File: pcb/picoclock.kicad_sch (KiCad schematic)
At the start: 63 parts, among them J1 UART, J10 USB, J11 Alt Power, J12 PWM, J2 AUDIO, J3 xx, J4 xx, J5 Power In, J6 USB_C_Receptacle, J7 xx, J8 xx, J9 screen_adapter_connector, SW1 SW_Push, SW2 SW_Push, SW3 SW_Push, SW4 SW_Push, SW5 SW_Push, SW6 SW_Push, U1 PCF8563T, U2 Pico, U3 MCP9808_MSOP, U4 PCM5100, Y1 Crystal

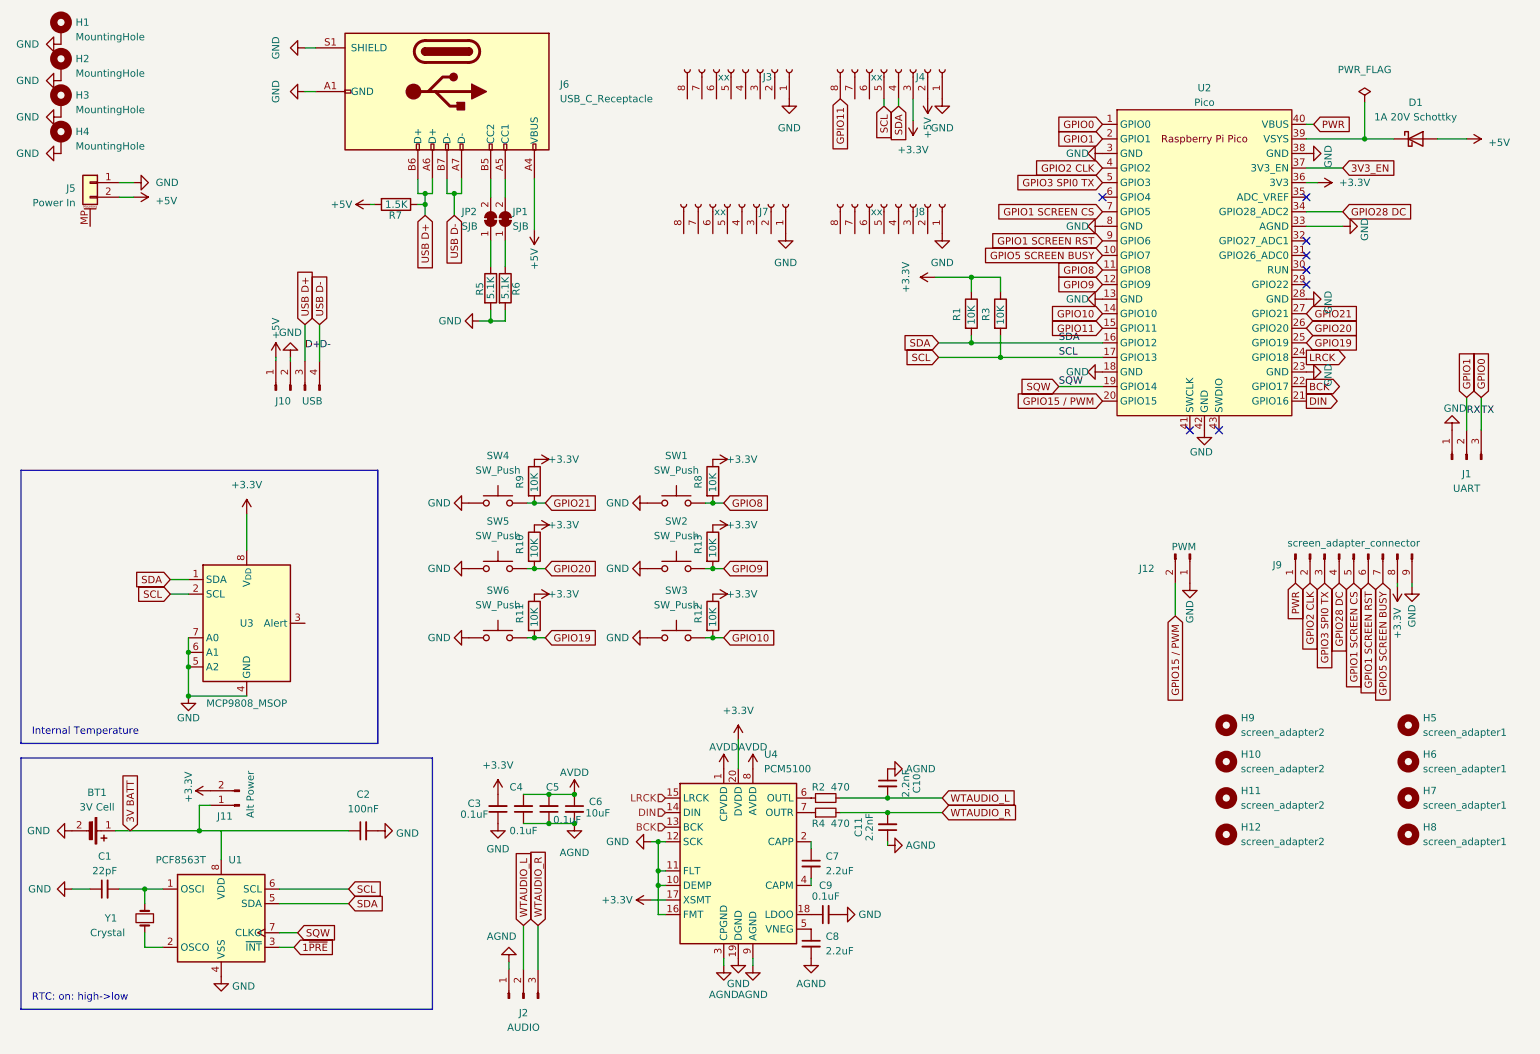
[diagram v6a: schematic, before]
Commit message: [pcb] fix PCM5100 layout, AVDD, improvements
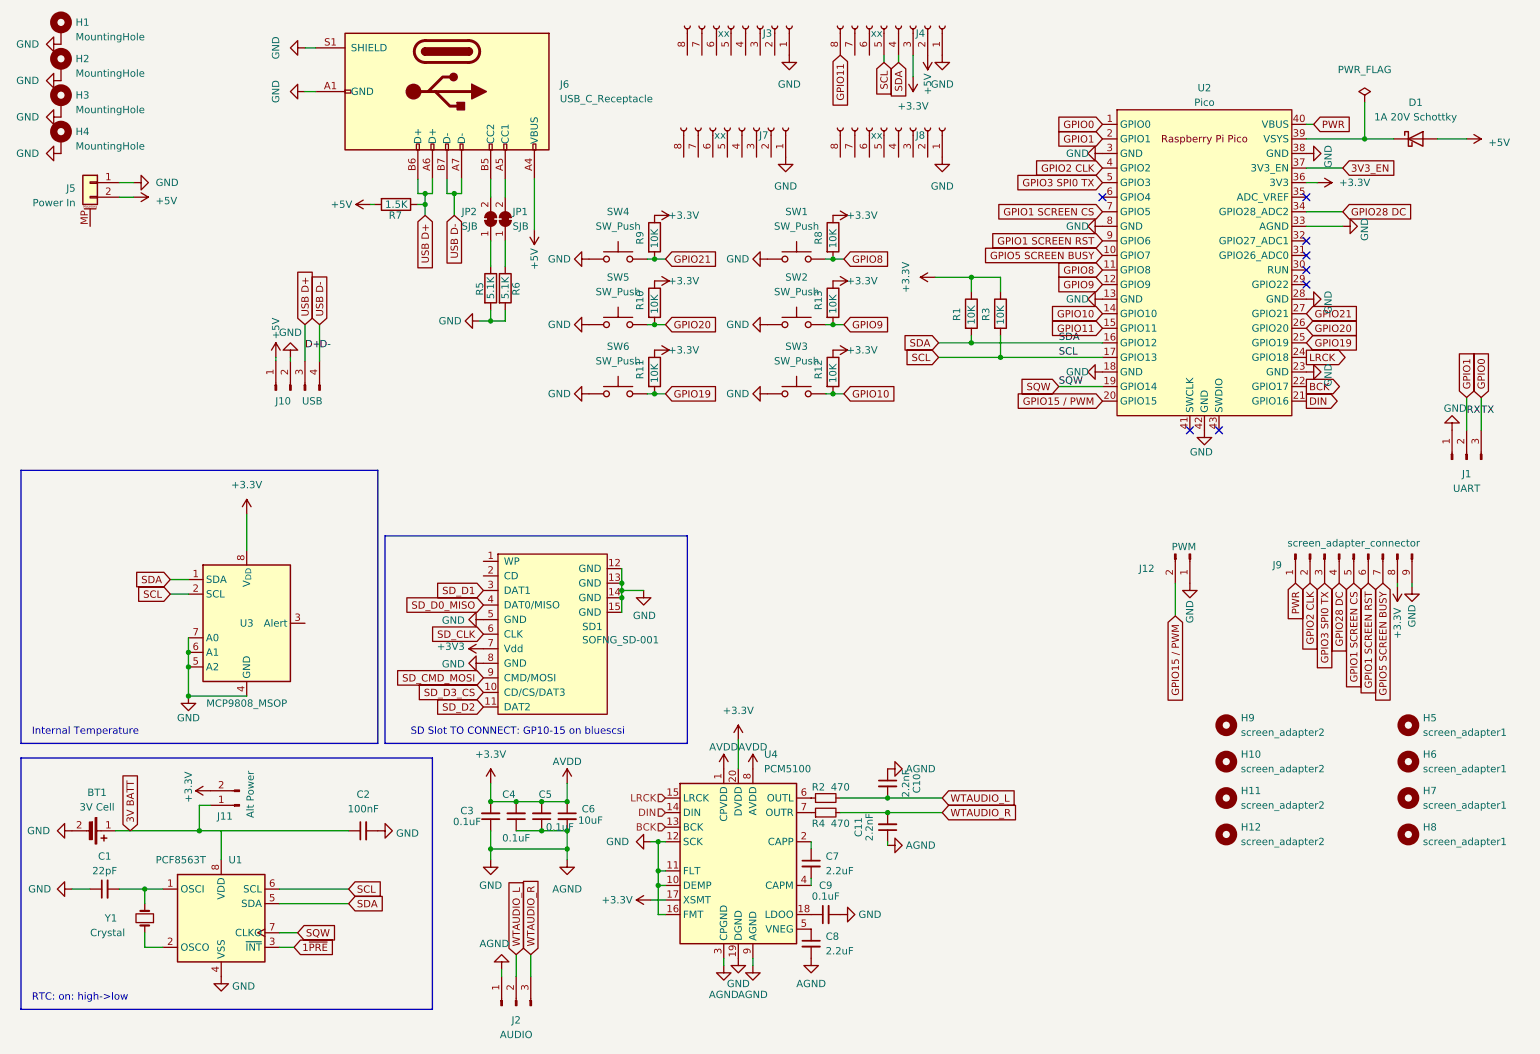
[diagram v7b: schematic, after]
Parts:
- added SD1: SOFNG_SD-001, CustomFootprints:SOFNG_SD-001, symbol custom_symbols:SOFNG_SD-001
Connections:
- net AVDD is gone; now on net +3.3V: C4.2, C5.2, C6.1, U4.1 (CPVDD), U4.8 (AVDD)
- net GND is gone; now on net AGND: BT1.2 (-), C1.1, C2.2, C3.1, C9.2, H1.1, H2.1, H3.1, H4.1, J1.1 (Pin_1), J10.2 (Pin_2), J12.1 (Pin_1), J3.1 (Pin_1), J4.1 (Pin_1), J5.1 (Pin_1), J6.A1 (GND), J6.A12 (GND), J6.B1 (GND), J6.B12 (GND), J6.S1 (SHIELD), J7.1 (Pin_1), J8.1 (Pin_1), J9.9 (Pin_9), R5.2, R6.2, SW1.1, SW2.1, SW3.1, SW4.1, SW5.1, SW6.1, U1.4 (VSS), U2.13 (GND), U2.18 (GND), U2.23 (GND), U2.28 (GND), U2.3 (GND), U2.33 (AGND), U2.38 (GND), U2.42 (GND), U2.8 (GND), U3.4 (GND), U3.5 (A2), U3.6 (A1), U3.7 (A0), U4.10 (DEMP), U4.11 (FLT), U4.12 (SCK), U4.16 (FMT), U4.19 (DGND)
- net AGND: now also SD1.12 (GND), SD1.13 (GND), SD1.14 (GND), SD1.15 (GND), SD1.5 (GND), SD1.8 (GND)
- new net +3V3: SD1.7 (Vdd)
- new net SD_CLK: SD1.6 (CLK)
- new net SD_CMD_MOSI: SD1.9 (CMD/MOSI)
- new net SD_D0_MISO: SD1.4 (DAT0/MISO)
- new net SD_D1: SD1.3 (DAT1)
- new net SD_D2: SD1.11 (DAT2)
- new net SD_D3_CS: SD1.10 (CD/CS/DAT3)
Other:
- note added: "SD Slot TO CONNECT: GP10-15 on bluescsi"
- moved on the sheet: C3, C4, C5, C6, J2, J3, J4, J7, J8, R10, R11, R12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

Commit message: [pcb] add sdcard: had to move PCM5100, other
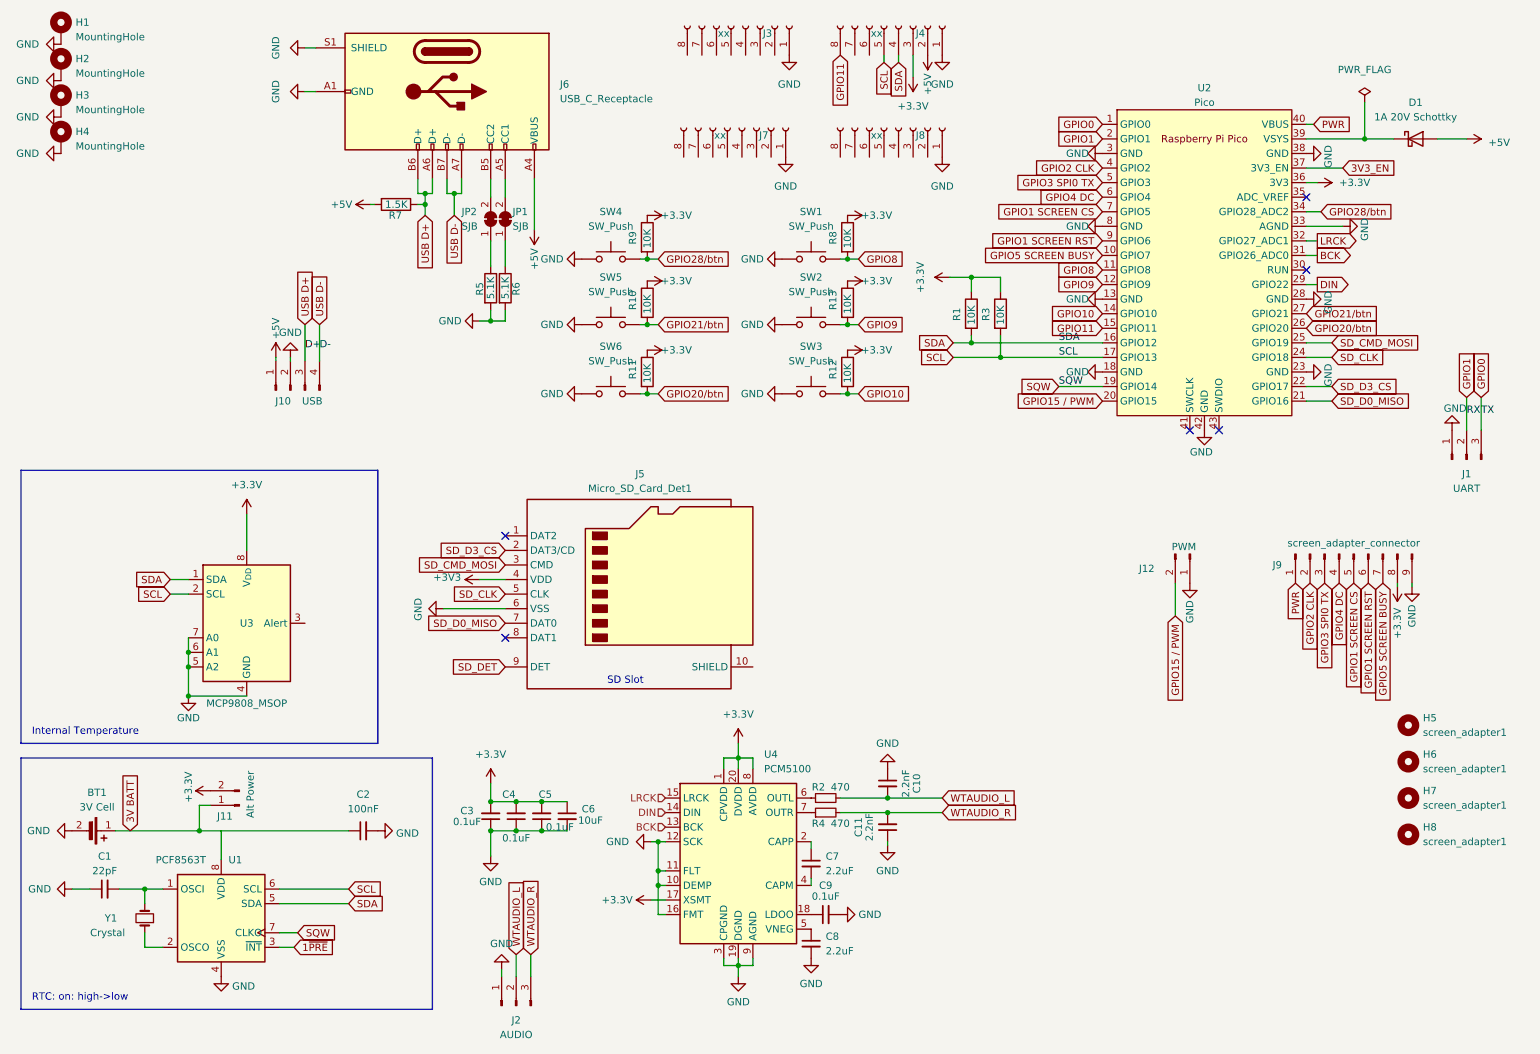
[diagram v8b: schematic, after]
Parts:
- removed H10, H11, H12, H9: screen_adapter2, MountingHole:MountingHole_3mm, symbol Mechanical:MountingHole
- removed J5: Power In, Connector_BarrelJack:BarrelJack_CUI_PJ-102AH_Horizontal, symbol Connector_Generic_MountingPin:Conn_01x02_MountingPin
- removed SD1: SOFNG_SD-001, CustomFootprints:SOFNG_SD-001, symbol custom_symbols:SOFNG_SD-001
- added J5: Micro_SD_Card_Det1, symbol Connector:Micro_SD_Card_Det1
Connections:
- net +3V3: now also J5.4 (VDD)
- net BCK: now also U2.31 (GPIO26_ADC0); no longer U2.22 (GPIO17)
- net DIN: now also U2.29 (GPIO22); no longer U2.21 (GPIO16)
- net LRCK: now also U2.32 (GPIO27_ADC1); no longer U2.24 (GPIO18)
- net SD_CLK: now also U2.24 (GPIO18), J5.5 (CLK)
- net SD_CMD_MOSI: now also U2.25 (GPIO19), J5.3 (CMD)
- net SD_D0_MISO: now also U2.21 (GPIO16), J5.7 (DAT0)
- net SD_D3_CS: now also U2.22 (GPIO17), J5.2 (DAT3/CD)
- net GPIO4 DC: now reaches U2.6 (GPIO4)
- net GPIO4 DC: now also J9.4 (Pin_4)
- net AGND renamed GND
- net GND: now also J5.6 (VSS)
- net GPIO19 renamed GPIO20/btn
- net GPIO20/btn: now also U2.26 (GPIO20); no longer U2.25 (GPIO19)
- net GPIO20 renamed GPIO21/btn
- net GPIO21/btn: now also U2.27 (GPIO21); no longer U2.26 (GPIO20)
- net GPIO21 renamed GPIO28/btn
- net GPIO28/btn: now also U2.34 (GPIO28_ADC2); no longer U2.27 (GPIO21)
- removed net GPIO28 DC: J9.4 (Pin_4), U2.34 (GPIO28_ADC2)
- new net SD_DET: J5.9 (DET)
- no-connect marks 8 -> 6
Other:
- note added: "SD Slot"
- note removed: "SD Slot TO CONNECT: GP10-15 on bluescsi"
- moved on the sheet: R10, R11, R12, R13, R8, R9, SW1, SW2, SW3, SW4, SW5, SW6
